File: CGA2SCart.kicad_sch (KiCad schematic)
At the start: 25 parts, among them J1 SCART-F, J2 DB9_Male, J3 Audio-Jack-3_2Switches, Q1 2N7000

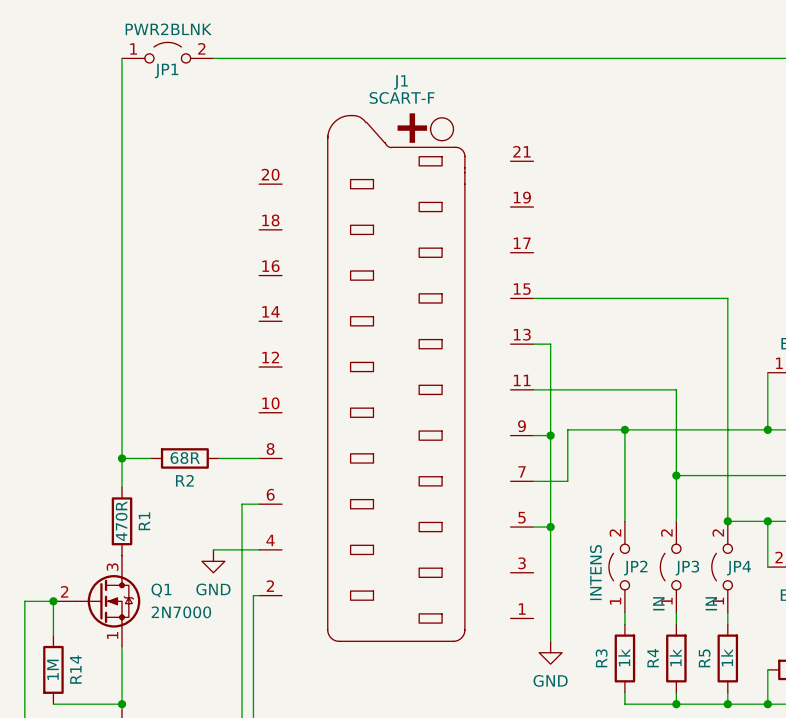
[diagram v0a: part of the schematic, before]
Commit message: Corrected sync problem
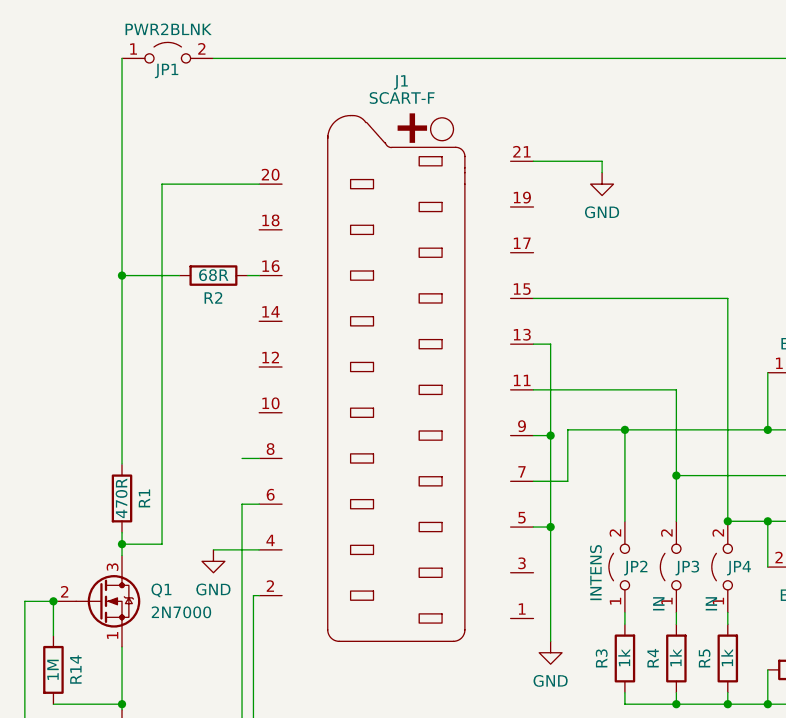
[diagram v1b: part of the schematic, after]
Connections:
- net GND: now also J1.21 (P21)
- net at J1.16 (P16): now also R2.1
- net at J1.20 (P20): now also Q1.3 (D), R1.2
- net at J1.8 (P8): no longer R2.1
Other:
- moved on the sheet: R1, R2
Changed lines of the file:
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@@
   (junction (at 142.875 102.87) (diameter 0) (color 0 0 0 0)
   )
-  (junction (at 95.25 95.25) (diameter 0) (color 0 0 0 0)
-  )
   (junction (at 156.845 97.155) (diameter 0) (color 0 0 0 0)
   )
@@
   (junction (at 167.005 122.555) (diameter 0) (color 0 0 0 0)
   )
+  (junction (at 95.25 74.93) (diameter 0) (color 0 0 0 0)
+  )
   (junction (at 162.56 102.235) (diameter 0) (color 0 0 0 0)
   )
+  (junction (at 95.25 104.775) (diameter 0) (color 0 0 0 0)
+  )
   (wire (pts (xy 189.23 97.155) (xy 210.185 97.155))
     (stroke (width 0) (type default) (color 0 0 0 0))
@@
     (stroke (width 0) (type default) (color 0 0 0 0))
   )
-  (wire (pts (xy 95.25 98.425) (xy 95.25 95.25))
+  (wire (pts (xy 95.25 74.93) (xy 95.25 95.885))
     (stroke (width 0) (type default) (color 0 0 0 0))
   )
@@
     (stroke (width 0) (type default) (color 0 0 0 0))
   )
+  (wire (pts (xy 95.25 103.505) (xy 95.25 104.775))
+    (stroke (width 0) (type default) (color 0 0 0 0))
+  )
   (wire (pts (xy 174.625 118.745) (xy 179.07 118.745))
     (stroke (width 0) (type default) (color 0 0 0 0))
   )
-  (wire (pts (xy 95.25 95.25) (xy 98.425 95.25))
+  (wire (pts (xy 148.59 63.5) (xy 148.59 62.23))
     (stroke (width 0) (type default) (color 0 0 0 0))
   )
@@
     (stroke (width 0) (type default) (color 0 0 0 0))
   )
+  (wire (pts (xy 95.25 74.93) (xy 101.6 74.93))
+    (stroke (width 0) (type default) (color 0 0 0 0))
+  )
   (wire (pts (xy 105.41 50.8) (xy 209.55 50.8))
     (stroke (width 0) (type default) (color 0 0 0 0))
@@
     (stroke (width 0) (type default) (color 0 0 0 0))
   )
-  (wire (pts (xy 95.25 95.25) (xy 95.25 50.8))
-    (stroke (width 0) (type default) (color 0 0 0 0))
-  )
   (wire (pts (xy 162.56 122.555) (xy 167.005 122.555))
     (stroke (width 0) (type default) (color 0 0 0 0))
   )
+  (wire (pts (xy 109.22 74.93) (xy 110.49 74.93))
+    (stroke (width 0) (type default) (color 0 0 0 0))
+  )
   (wire (pts (xy 208.915 109.855) (xy 208.915 112.395))
     (stroke (width 0) (type default) (color 0 0 0 0))
@@
     (stroke (width 0) (type default) (color 0 0 0 0))
   )
+  (wire (pts (xy 99.695 64.77) (xy 110.49 64.77))
+    (stroke (width 0) (type default) (color 0 0 0 0))
+  )
   (wire (pts (xy 208.915 112.395) (xy 186.055 112.395))
     (stroke (width 0) (type default) (color 0 0 0 0))
@@
     (stroke (width 0) (type default) (color 0 0 0 0))
   )
+  (wire (pts (xy 148.59 62.23) (xy 140.97 62.23))
+    (stroke (width 0) (type default) (color 0 0 0 0))
+  )
   (wire (pts (xy 104.14 149.86) (xy 108.585 149.86))
     (stroke (width 0) (type default) (color 0 0 0 0))
@@
     (stroke (width 0) (type default) (color 0 0 0 0))
   )
-  (wire (pts (xy 106.045 95.25) (xy 110.49 95.25))
+  (wire (pts (xy 95.25 104.775) (xy 99.695 104.775))
+    (stroke (width 0) (type default) (color 0 0 0 0))
+  )
+  (wire (pts (xy 108.585 95.25) (xy 110.49 95.25))
     (stroke (width 0) (type default) (color 0 0 0 0))
   )
@@
     (stroke (width 0) (type default) (color 0 0 0 0))
   )
+  (wire (pts (xy 99.695 104.775) (xy 99.695 64.77))
+    (stroke (width 0) (type default) (color 0 0 0 0))
+  )
+  (wire (pts (xy 95.25 104.775) (xy 95.25 106.045))
+    (stroke (width 0) (type default) (color 0 0 0 0))
+  )
   (wire (pts (xy 84.455 136.525) (xy 191.77 136.525))
     (stroke (width 0) (type default) (color 0 0 0 0))
@@
   )
   (wire (pts (xy 140.97 102.87) (xy 142.875 102.87))
+    (stroke (width 0) (type default) (color 0 0 0 0))
+  )
+  (wire (pts (xy 95.25 74.93) (xy 95.25 50.8))
     (stroke (width 0) (type default) (color 0 0 0 0))
   )
@@
     (pin "2")
   )
-  (symbol (lib_id "Device:R") (at 102.235 95.25 270) (unit 1)
-    (in_bom yes) (on_board yes)
-    (property "Reference" "R2" (id 0) (at 102.235 97.79 90))
-    (property "Value" "68R" (id 1) (at 102.235 95.25 90))
-    (property "Footprint" "Resistor_THT:R_Axial_DIN0207_L6.3mm_D2.5mm_P7.62mm_Horizontal" (id 2) (at 102.235 93.472 90)
-      (effects (font (size 1.27 1.27)) hide)
-    )
-    (property "Datasheet" "~" (id 3) (at 102.235 95.25 0)
+  (symbol (lib_id "Device:R") (at 105.41 74.93 270) (unit 1)
+    (in_bom yes) (on_board yes)
+    (property "Reference" "R2" (id 0) (at 105.41 77.47 90))
+    (property "Value" "68R" (id 1) (at 105.41 74.93 90))
+    (property "Footprint" "Resistor_THT:R_Axial_DIN0207_L6.3mm_D2.5mm_P7.62mm_Horizontal" (id 2) (at 105.41 73.152 90)
+      (effects (font (size 1.27 1.27)) hide)
+    )
+    (property "Datasheet" "~" (id 3) (at 105.41 74.93 0)
       (effects (font (size 1.27 1.27)) hide)
     )
@@
   (symbol (lib_id "power:GND") (at 105.41 105.41 0) (unit 1)
     (in_bom yes) (on_board yes) (fields_autoplaced)
-    (property "Reference" "#PWR?" (id 0) (at 105.41 111.76 0)
+    (property "Reference" "#PWR0105" (id 0) (at 105.41 111.76 0)
       (effects (font (size 1.27 1.27)) hide)
     )
@@
     (pin "2")
   )
-  (symbol (lib_id "Device:R") (at 95.25 102.235 0) (unit 1)
-    (in_bom yes) (on_board yes)
-    (property "Reference" "R1" (id 0) (at 97.79 102.235 90))
-    (property "Value" "470R" (id 1) (at 95.25 102.235 90))
-    (property "Footprint" "Resistor_THT:R_Axial_DIN0207_L6.3mm_D2.5mm_P7.62mm_Horizontal" (id 2) (at 93.472 102.235 90)
-      (effects (font (size 1.27 1.27)) hide)
-    )
-    (property "Datasheet" "~" (id 3) (at 95.25 102.235 0)
+  (symbol (lib_id "Device:R") (at 95.25 99.695 0) (unit 1)
+    (in_bom yes) (on_board yes)
+    (property "Reference" "R1" (id 0) (at 97.79 99.695 90))
+    (property "Value" "470R" (id 1) (at 95.25 99.695 90))
+    (property "Footprint" "Resistor_THT:R_Axial_DIN0207_L6.3mm_D2.5mm_P7.62mm_Horizontal" (id 2) (at 93.472 99.695 90)
+      (effects (font (size 1.27 1.27)) hide)
+    )
+    (property "Datasheet" "~" (id 3) (at 95.25 99.695 0)
       (effects (font (size 1.27 1.27)) hide)
     )
@@
     (pin "2")
   )
+  (symbol (lib_id "power:GND") (at 148.59 63.5 0) (unit 1)
+    (in_bom yes) (on_board yes) (fields_autoplaced)
+    (property "Reference" "#PWR0106" (id 0) (at 148.59 69.85 0)
+      (effects (font (size 1.27 1.27)) hide)
+    )
+    (property "Value" "GND" (id 1) (at 148.59 67.945 0))
+    (property "Footprint" "" (id 2) (at 148.59 63.5 0)
+      (effects (font (size 1.27 1.27)) hide)
+    )
+    (property "Datasheet" "" (id 3) (at 148.59 63.5 0)
+      (effects (font (size 1.27 1.27)) hide)
+    )
+    (pin "1")
+  )
   (symbol (lib_id "Jumper:Jumper_2_Open") (at 151.13 107.315 90) (unit 1)
     (in_bom yes) (on_board yes)
@@
     )
     (path "/76210b7e-8272-4a92-8aa8-8831ed0fa887"
-      (reference "#PWR?") (unit 1) (value "GND") (footprint "")
+      (reference "#PWR0105") (unit 1) (value "GND") (footprint "")
+    )
+    (path "/d32b7061-575b-4e35-b5c0-0a0f382d9f10"
+      (reference "#PWR0106") (unit 1) (value "GND") (footprint "")
     )
     (path "/1799c71f-013d-402a-b710-c5585561a246"

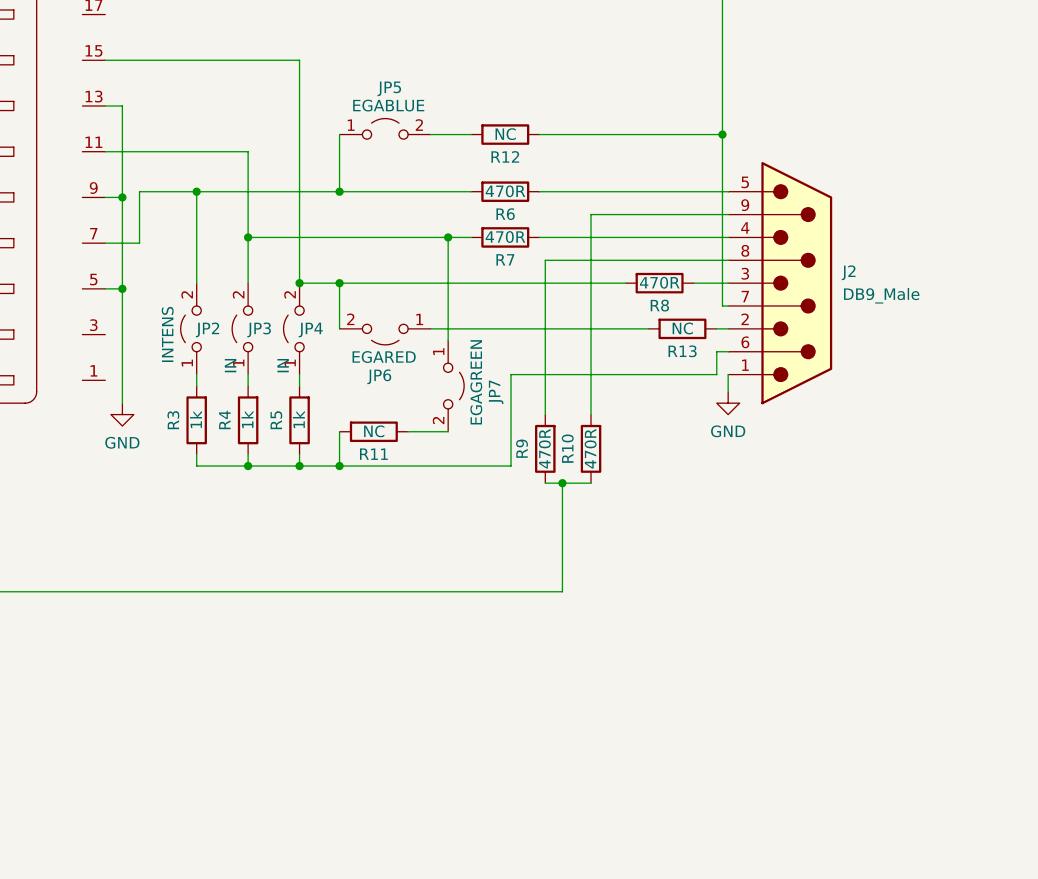
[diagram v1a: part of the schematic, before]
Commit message: Added a VGA port
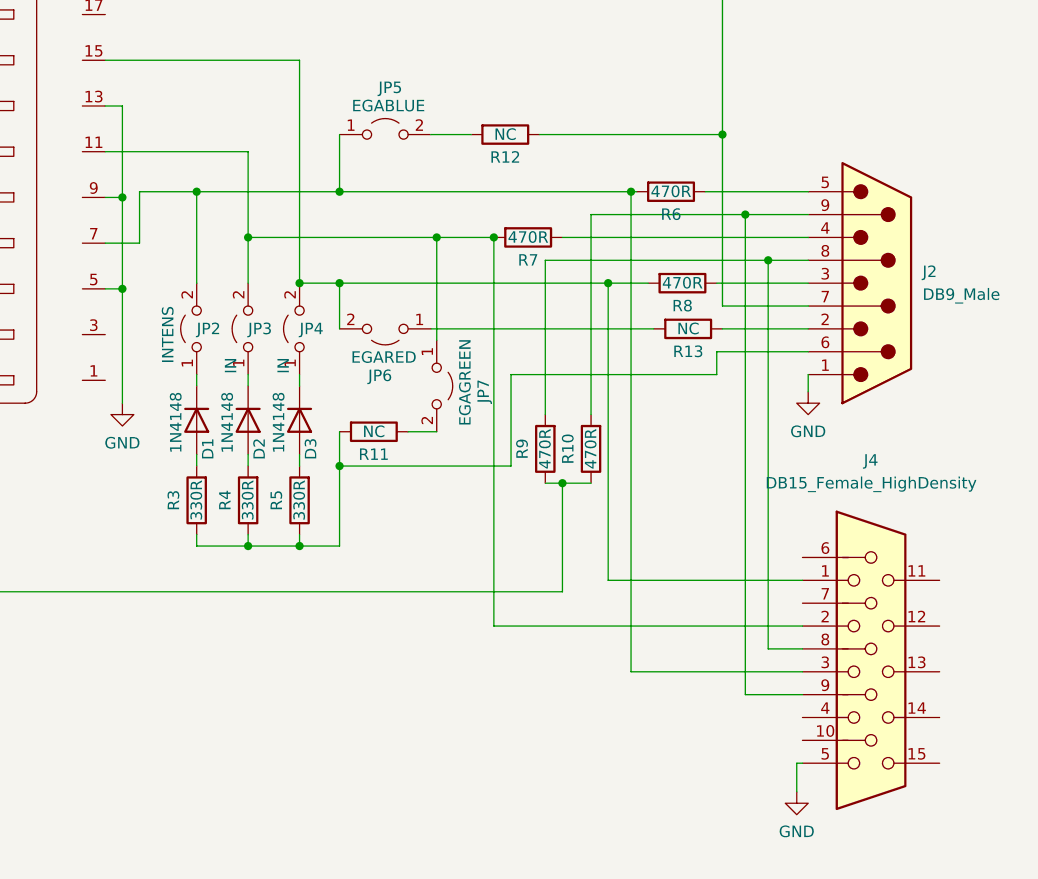
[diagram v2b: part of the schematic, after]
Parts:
- added D1, D2, D3: 1N4148, Diode_THT:D_DO-35_SOD27_P7.62mm_Horizontal, symbol Device:D
- added J4: DB15_Female_HighDensity, Connector_Dsub:DSUB-15-HD_Female_Horizontal_P2.29x1.98mm_EdgePinOffset3.03mm_Housed_MountingHolesOffset4.94mm, symbol Connector:DB15_Female_HighDensity
- R3, R4, R5: value 1k -> 330R
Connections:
- net GND: now also J4.5
- net at J1.11 (P11), JP3.2 (B), JP7.1 (A)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: now also J4.2
- net at J1.15 (P15), JP4.2 (B), JP6.2 (B)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: now also J4.1
- net at J1.7 (P7), JP2.2 (B), JP5.1 (A)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: now also J4.3
- net at R3.2: now also D1.2 (A); no longer JP2.1 (A)
- net at J2.8, R9.2: now also J4.8
- net at J2.9, R10.2: now also J4.9
- net at JP4.1 (A): now also D3.1 (K); no longer R5.2
- net at JP3.1 (A): now also D2.1 (K); no longer R4.2
- new net: D1.1 (K), JP2.1 (A)
- new net: D3.2 (A), R5.2
- new net: D2.2 (A), R4.2
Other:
- moved on the sheet: J2, JP7, R13, R3, R4, R5, R6, R7, R8

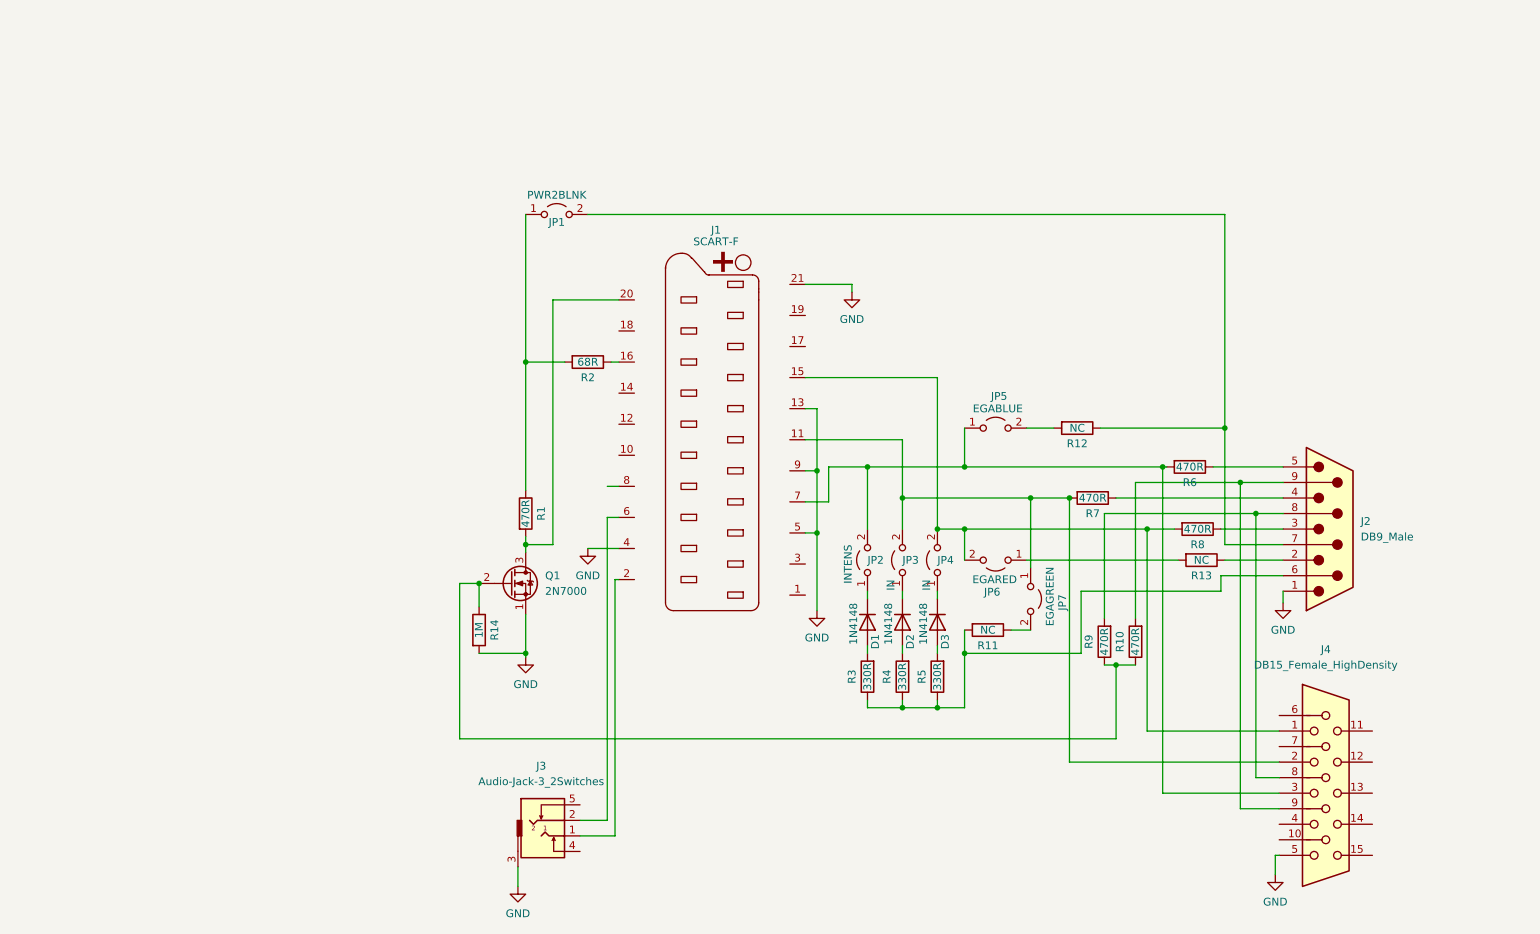
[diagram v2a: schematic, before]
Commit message: Fixed problem with VGA pins...
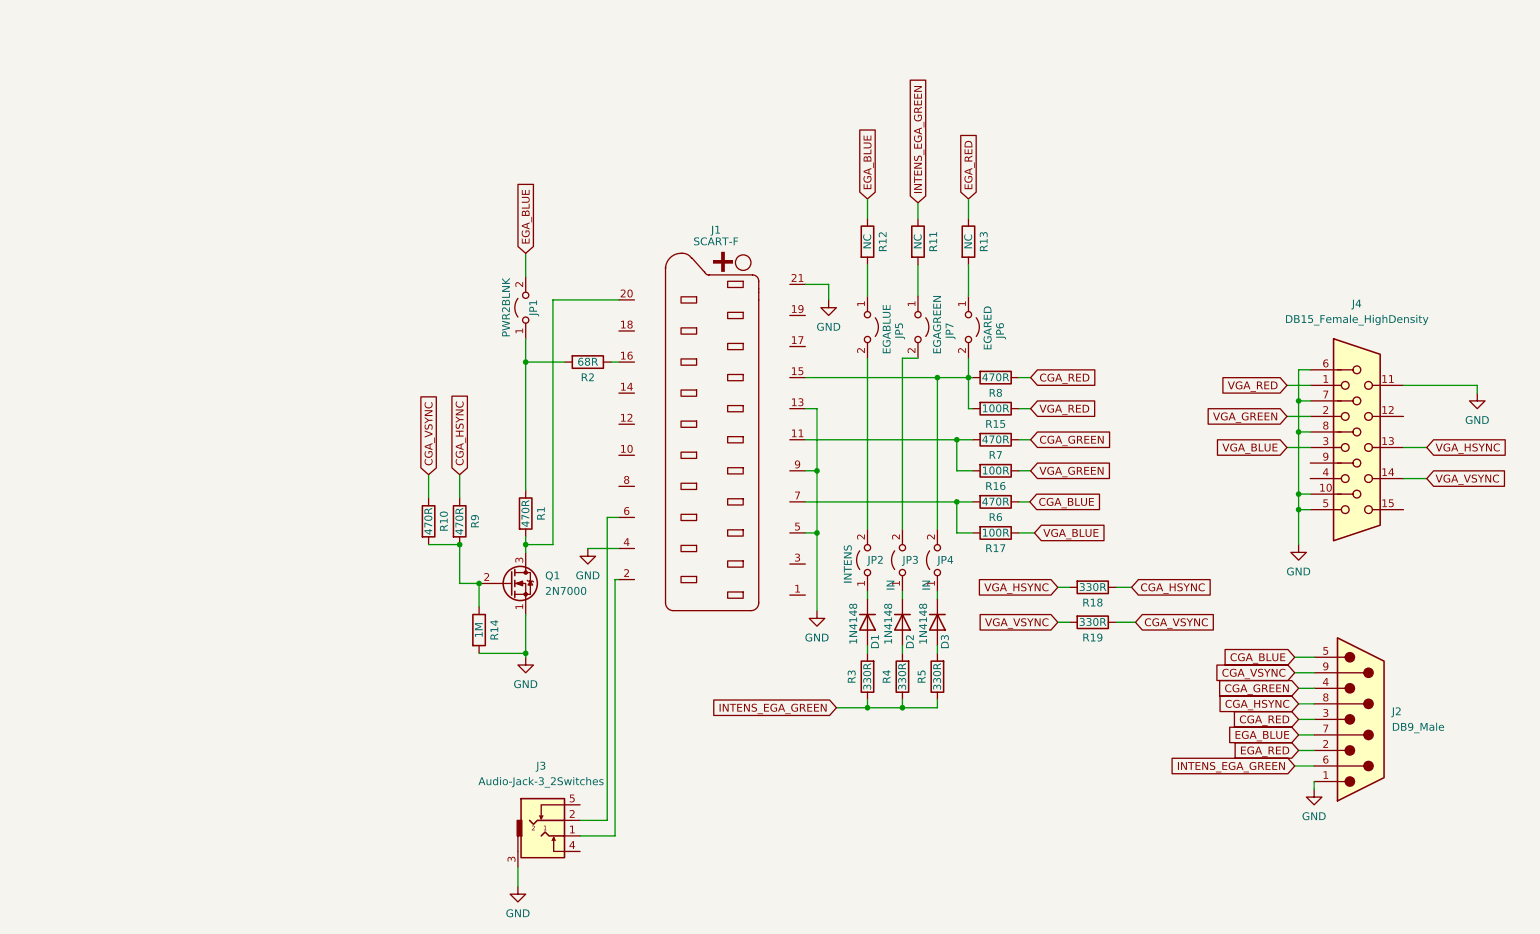
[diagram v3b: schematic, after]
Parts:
- added R15, R16, R17: 100R, Resistor_THT:R_Axial_DIN0207_L6.3mm_D2.5mm_P7.62mm_Horizontal, symbol Device:R
- added R18, R19: 330R, Resistor_THT:R_Axial_DIN0207_L6.3mm_D2.5mm_P7.62mm_Horizontal, symbol Device:R
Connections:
- net GND: now also J4.10, J4.11, J4.6, J4.7, J4.8
- net at J1.15 (P15), JP4.2 (B), JP6.2 (B)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: now also R15.2; no longer J4.1
- net CGA_RED: now reaches J2.3, R8.1
- net at R12.2: now also JP5.1 (A); no longer JP5.2 (B)
- net EGA_BLUE: now reaches J2.7, JP1.2 (B), R12.1
- net at Q1.2 (G), R14.1: now also R10.2, R9.2; no longer R10.1, R9.1
- net INTENS_EGA_GREEN: now reaches J2.6, R3.1, R4.1, R5.1
- net INTENS_EGA_GREEN: now also R11.1; no longer R11.2
- net VGA_HSYNC: now reaches J4.13
- net VGA_HSYNC: now also R18.2
- net VGA_VSYNC: now reaches J4.14
- net VGA_VSYNC: now also R19.2
- net EGA_RED: now reaches J2.2, R13.1
- net CGA_GREEN: now reaches J2.4, R7.1
- net CGA_BLUE: now reaches J2.5, R6.1
- net at JP7.2 (B): now also JP3.2 (B); no longer R11.1
- new net: J1.11 (P11), R16.2, R7.2
- new net: J1.7 (P7), R17.2, R6.2
- new net: JP2.2 (B), JP5.2 (B)
- new net: JP7.1 (A), R11.2
- new net CGA_HSYNC: J2.8, R18.1, R9.1
- new net CGA_VSYNC: J2.9, R10.1, R19.1
- new net VGA_BLUE: J4.3, R17.1
- new net VGA_GREEN: J4.2, R16.1
- new net VGA_RED: J4.1, R15.1
- now unconnected: J4.9
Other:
- moved on the sheet: J2, J4, JP1, JP5, JP6, JP7, R10, R11, R12, R13, R6, R7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
